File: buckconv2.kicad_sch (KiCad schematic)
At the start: 0 parts

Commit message: feat: 48-5v buck converter
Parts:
- added Cboot2: 470nF, 20mOhm, Capacitor_SMD:C_0805_2012Metric_Pad1.18x1.45mm_HandSolder, symbol Device:C
- added Cin2: 4.7uF, 5.89mOhm, Capacitor_SMD:C_0805_2012Metric_Pad1.18x1.45mm_HandSolder, symbol Device:C
- added Cinx2: 470nF, 33.996mOhm, Capacitor_SMD:C_0805_2012Metric_Pad1.18x1.45mm_HandSolder, symbol Device:C
- added Cout2: 150uF, Capacitor_SMD:C_0805_2012Metric_Pad1.18x1.45mm_HandSolder, symbol Device:C_Polarized_US
- added Coutx2: 470nF, 57.491mOhm, Capacitor_SMD:C_0805_2012Metric_Pad1.18x1.45mm_HandSolder, symbol Device:C
- added Cvcc2: 2.2uF, 7.674mOhm, Capacitor_SMD:C_0805_2012Metric_Pad1.18x1.45mm_HandSolder, symbol Device:C
- added L2: 5.6uH, Inductor_SMD:L_6.3x6.3_H3, symbol Device:L
- added Rfbb2: 24.9k, Resistor_SMD:R_0201_0603Metric, symbol Device:R
- added Rfbt2, Rpgood2: 100kOhm, Resistor_SMD:R_0201_0603Metric, symbol Device:R
- added U3: LM76005, Package_DFN_QFN:Texas_RNP0030B_WQFN-30-1EP_4x6mm_P0.5mm_EP1.8x4.5mm_ThermalVias, symbol Regulator_Switching:LM76005
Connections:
- new net: Rfbb2.1, Rfbt2.2, U3.12 (FB)
- new net: Cvcc2.1, U3.8 (VCC)
- new net: Cboot2.1, U3.6 (BOOT)
- new net: Cboot2.2, L2.1, U3.1 (SW), U3.2 (SW), U3.3 (SW), U3.4 (SW), U3.5 (SW)
- new net: Rpgood2.1, U3.16 (PGOOD)
- new net +5V: Cout2.1, Coutx2.1, L2.2, Rfbt2.1, Rpgood2.2
- new net GND: Cin2.2, Cinx2.2, Cout2.2, Coutx2.2, Cvcc2.2, Rfbb2.2, U3.13 (AGND), U3.14 (AGND), U3.15 (AGND), U3.17 (SYNC/MODE), U3.19 (NC_{GND}), U3.24 (PGND), U3.25 (PGND), U3.26 (PGND), U3.27 (NC_{GND}), U3.28 (NC_{GND}), U3.29 (NC_{GND}), U3.30 (NC_{GND}), U3.31 (AGND), U3.9 (BIAS)
- new net V_switched: Cin2.1, Cinx2.1, U3.18 (EN), U3.20 (PVIN), U3.21 (PVIN), U3.22 (PVIN)
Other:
- company: (none) -> UMass Robotics
- title: (none) -> 48v to 5v Buck Converter

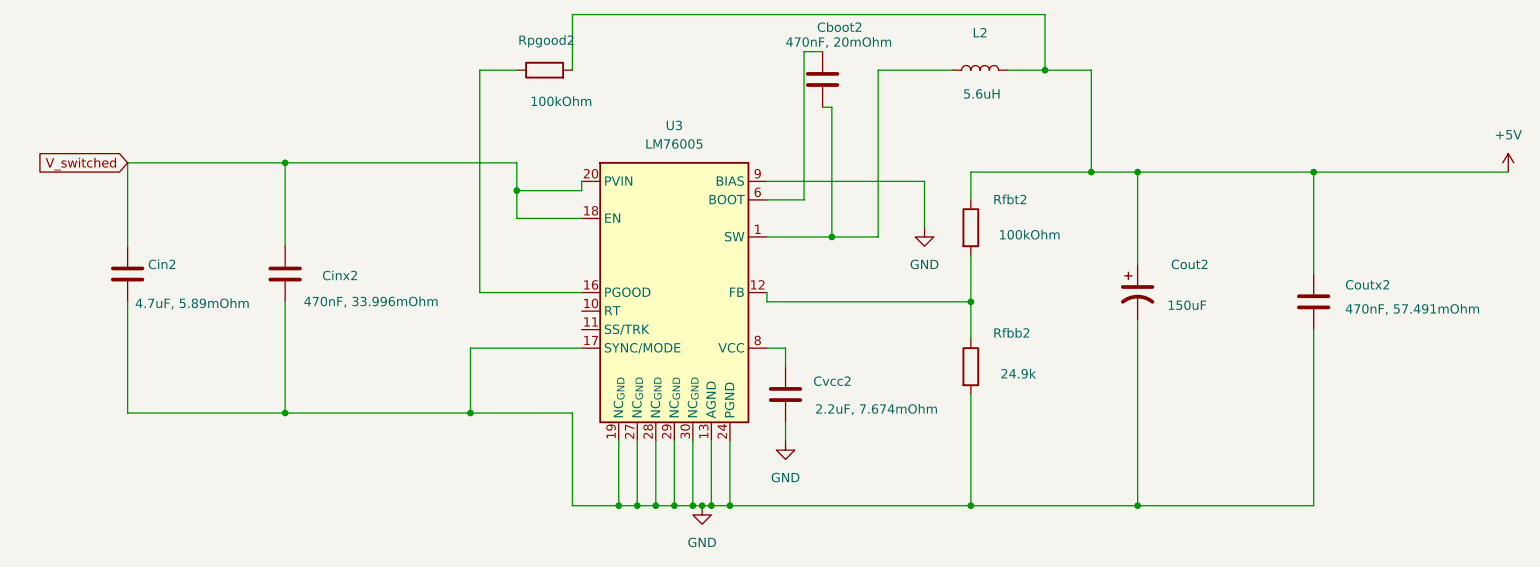
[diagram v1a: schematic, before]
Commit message: Fixed ERC
Created Buck3
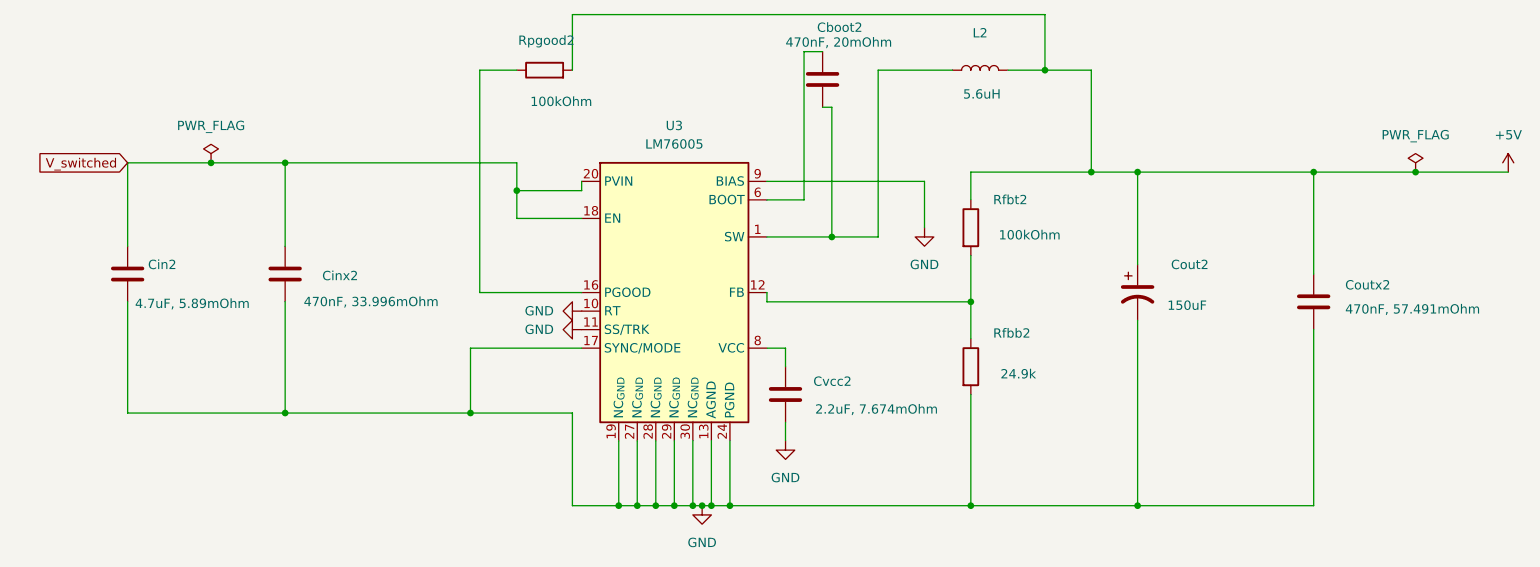
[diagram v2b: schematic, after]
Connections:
- net GND: now also U3.10 (RT), U3.11 (SS/TRK)
